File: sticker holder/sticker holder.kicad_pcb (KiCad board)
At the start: 2 copper layers, 30 x 30 mm, 1 part

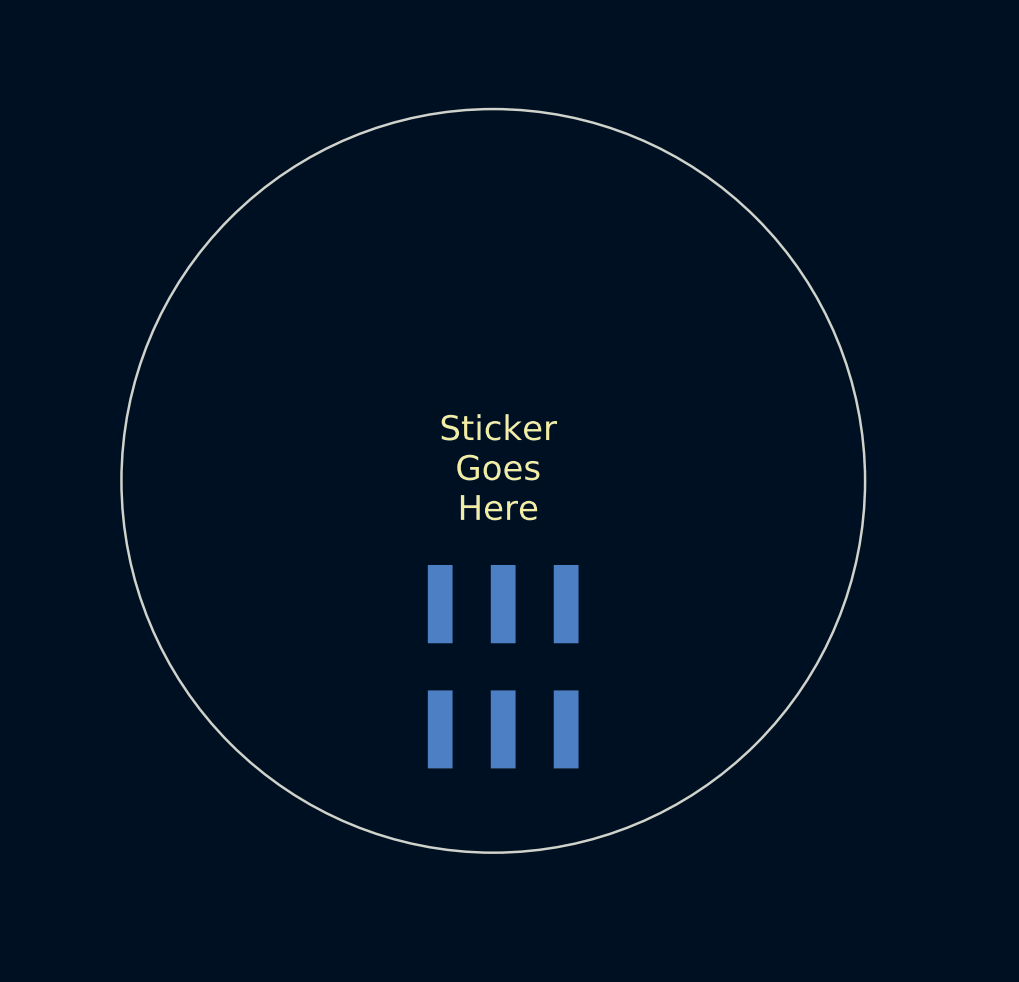
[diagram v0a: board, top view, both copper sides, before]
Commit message: updates to sticker holder SAO
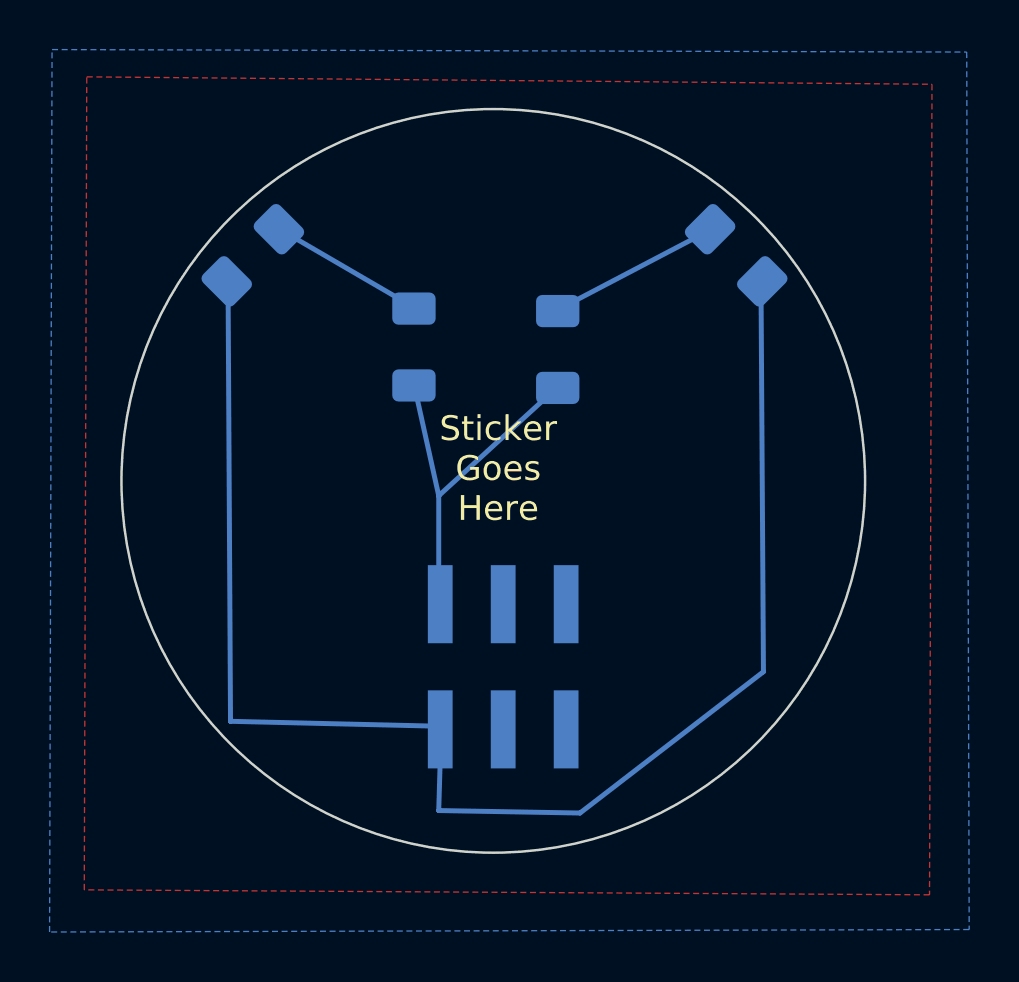
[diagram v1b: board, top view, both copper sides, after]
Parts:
- added D1: LED_1206_3216Metric_Pad1.42x1.75mm_HandSolder, LED_SMD:LED_1206_3216Metric_Pad1.42x1.75mm_HandSolder, B.Cu at (125.5, 72.0)
- added D2: LED_1206_3216Metric_Pad1.42x1.75mm_HandSolder, LED_SMD:LED_1206_3216Metric_Pad1.42x1.75mm_HandSolder, B.Cu at (106.0, 72.0)
- added R1: R_1206_3216Metric_Pad1.30x1.75mm_HandSolder, Resistor_SMD:R_1206_3216Metric_Pad1.30x1.75mm_HandSolder, B.Cu at (118.3, 75.8)
- added R2: R_1206_3216Metric_Pad1.30x1.75mm_HandSolder, Resistor_SMD:R_1206_3216Metric_Pad1.30x1.75mm_HandSolder, B.Cu at (112.5, 75.7)
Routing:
- added copper zone on B.Cu, net (none)
- added copper zone on F.Cu, net (none)
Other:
- board text added: "jlcjlcjlcjlc"
- board text added: "v1"
